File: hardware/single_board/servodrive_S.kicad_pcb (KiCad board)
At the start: 6 copper layers, 65 x 65 mm, 194 parts, among them J1 PhasePad_Arc, J12 USB-C, J13 EXPANSION, J14 RS485 IN, J15 RS485 OUT, J2 PhasePad_Arc, J3 PhasePad_Arc, J4 XT30, Q1 BSC030N08NS5, Q1001 2N7002, Q2 BSC030N08NS5, Q3 BSC030N08NS5, Q4 BSC030N08NS5, Q5 BSC030N08NS5, Q6 BSC030N08NS5, SW1 BOOTSEL, U1 EG2103, U10 MT6701, U11 LMR38010SDDAR, U12 LMR38010SDDAR, U13 USBLC6-2SC6, U14 SIT3088ETK, U15 SIT3088ETK, U17 SIT3088ETK, U18 SIT3088ETK, U2 EG2103, U3 EG2103, U4 INA241A3, U5 INA241A3, U6 INA241A3, U7 RP2350A, U8 W25Q16JVUXIQ, U9 SPX3819M5-3.3, Y1 12MHz

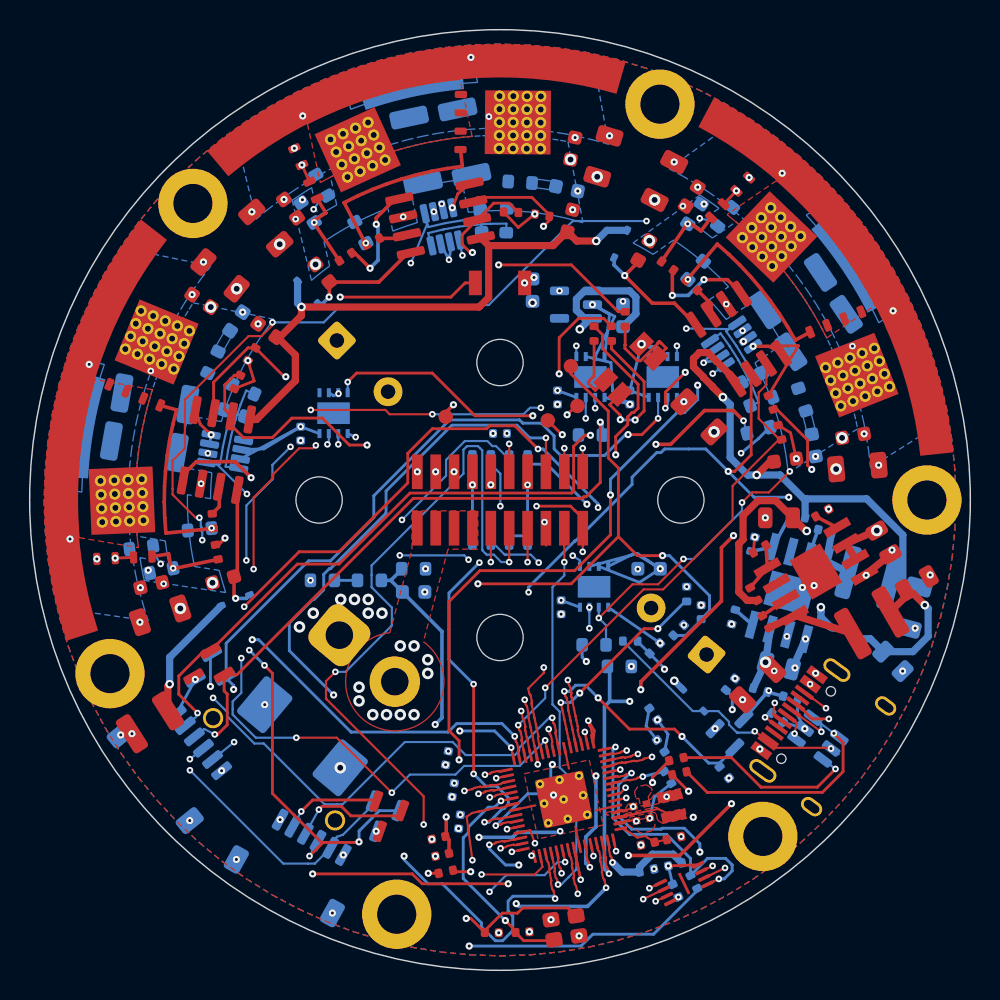
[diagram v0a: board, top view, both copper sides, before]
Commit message: Board S with six D6.3 bulk cans: routed, DRC 0; the bulk options page
The two D10 cans carried 6.4 A of ripple each at 20 A RMS per phase, 3.7
times their rating at 20-40 kHz. Six PA100V22M6X9 (22 uF, 2.6 A) carry
2.3 A each, within rating to 16 A per phase continuously, 0.15 W a can.

Routed with the maze making the RS-485 IN pair and the encoder's CS and DO
before the router, then targeted rip-ups for EXP_GP24, HIN_A and SWCLK.
2241 segments, 444 vias; DRC 0 all severities, ERC 0, parity 219 of the
same kinds as before, netlist diff and deadcheck clean. bulk.html has the
parts, the banks through the DC-link network, what fits and what routed.
ethernet.html: the can holes, and GPIO14 is port OUT's UART now.

Co-Authored-By: Claude Opus 5.5 (1M context) <noreply@anthropic.com>
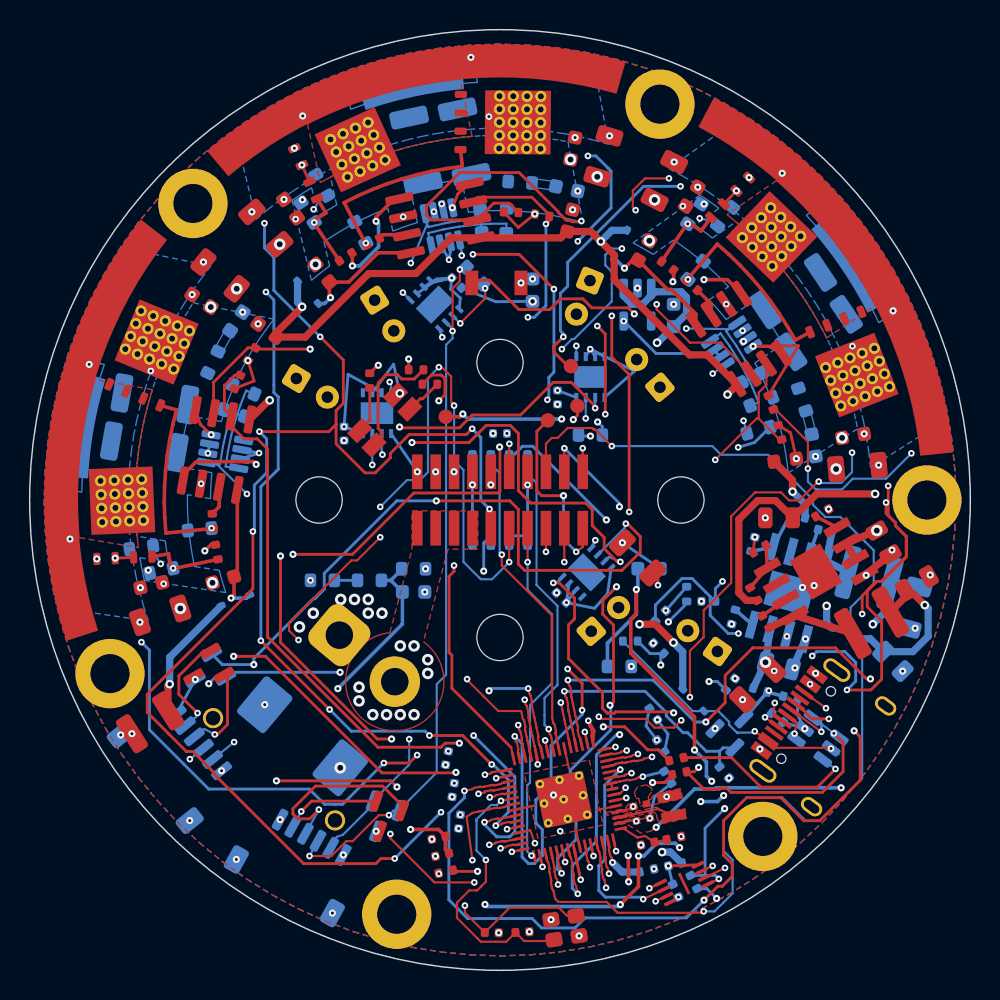
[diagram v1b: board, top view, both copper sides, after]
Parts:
- added C1012: 22u/100V polymer, Capacitor_THT:CP_Radial_D6.3mm_P2.50mm, F.Cu at (139.3, 91.2)
- added C1013: 22u/100V polymer, Capacitor_THT:CP_Radial_D6.3mm_P2.50mm, F.Cu at (154.2, 89.8)
- added C1014: 22u/100V polymer, Capacitor_THT:CP_Radial_D6.3mm_P2.50mm, F.Cu at (159.1, 97.2)
- added C1015: 22u/100V polymer, Capacitor_THT:CP_Radial_D6.3mm_P2.50mm, F.Cu at (154.3, 114.1)
- C1001, C1002: value 100u/100V polymer -> 22u/100V polymer; footprint Capacitor_THT:CP_Radial_D10.0mm_P5.00mm -> Capacitor_THT:CP_Radial_D6.3mm_P2.50mm
- moved R1105 26.8 mm to (146.2, 89.5), turned to 135 degrees
- moved C1102 23.5 mm to (145.0, 90.0), turned to 135 degrees
- moved U14 22.4 mm to (143.5, 91.5), turned to 45 degrees
- moved D1103 17.4 mm to (140.0, 99.5)
- moved R1107 15.8 mm to (139.0, 96.8)
- moved C1104 14.6 mm to (152.2, 111.8), turned to 135 degrees
- moved U17 14.5 mm to (154.0, 110.0), turned to 135 degrees
- moved R1109 14.2 mm to (143.2, 97.0), turned to 0 degrees
- moved R1108 13.7 mm to (142.2, 96.0), turned to 0 degrees
- moved C1007 10.6 mm to (157.5, 109.0)
- moved U9 4.25 mm to (157.5, 91.5), turned to -90 degrees
- moved C1001 3.84 mm to (133.9, 96.6), turned to -31 degrees
- moved C713 3.50 mm to (160.0, 92.2)
- moved C1103 3.00 mm to (137.2, 100.4)
- moved U15 3.00 mm to (139.5, 99.0)
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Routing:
- net RUN: track 60.2 -> 278.3 mm, vias 4 -> 18
- net SWCLK: track 45.6 -> 153.0 mm, vias 7 -> 11
- net RS485_IN_DN_P: track 129.1 -> 44.2 mm, vias 9 -> 3
- net RS485_IN_RX: track 14.4 -> 83.6 mm, vias 2 -> 4
- net ENC_DO: track 83.2 -> 21.5 mm, vias 8 -> 1
- net HIN_A: track 51.4 -> 110.2 mm, vias 5 -> 8
- net SWDIO: track 37.5 -> 95.6 mm, vias 4 -> 11
- net RS485_OUT_TX: track 47.0 -> 92.2 mm
- net RS485_IN_TX: track 48.0 -> 91.1 mm, vias 3 -> 7
- net ENC_SCK: track 69.1 -> 27.6 mm, vias 7 -> 2
- net LED_B: track 84.9 -> 46.3 mm, vias 4 -> 2
- net RS485_OUT_DN_P: track 79.4 -> 53.4 mm
- net RS485_IN_DN_N: track 73.3 -> 49.1 mm, vias 10 -> 4
- net EXP_GP20: track 48.8 -> 28.8 mm, vias 4 -> 2
- net +1V1: track 26.1 -> 45.9 mm, vias 4 -> 7
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
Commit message: Board S: SIT65HVD75ETK and W25Q80DVUXIE for the parts that went out of stock
Every placed part re-checked at JLCPCB on 2026-10-16: the SIT3088ETK and
the W25Q16JVUXIQ were at zero. The SIT65HVD75ETK is the same MAX3485
pinout in the same DFN-8 3x3 (C7433976, 20,671 in stock), and its receiver
threshold (V_IT+ <= -10 mV) reads a terminated idle pair as a 1, which
answers the fail-safe item on paper. The W25Q80DVUXIE is the same pins and
USON 2x3 land pattern, 8 Mbit (C401667, 8,611): firmware needs
PICO_FLASH_SIZE_BYTES 1 MB and has to set QE, which it ships clear.

Board S only (schematic_s overrides; board A keeps the W25Q16JV): two new
derived symbols appended to the library, the two sheets regenerated, the
routed board's value fields patched, the fan-out's escape rule taking the
new name. ERC 0, netlist == schematic_s, DRC 0 / 0 unconnected, schematic
parity the same 219 items as before. Viewer rebuilt.

Still short: the RP2350's 3.3 uH AOTA-B201610S3R3 (9) and TPSMF4L54A (42,
three a board).

Co-Authored-By: Claude Opus 5.5 <noreply@anthropic.com>
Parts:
- U14, U15, U17, U18: value SIT3088ETK -> SIT65HVD75ETK
- U8: value W25Q16JVUXIQ -> W25Q80DVUXIE
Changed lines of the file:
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@@
 			)
 		)
-		(property "Value" "W25Q16JVUXIQ"
+		(property "Value" "W25Q80DVUXIE"
 			(at 0 1.95 0)
 			(layer "F.Fab")
@@
 			)
 		)
-		(property "Value" "SIT3088ETK"
+		(property "Value" "SIT65HVD75ETK"
 			(at 0 0 0)
 			(layer "B.Fab")
@@
 			)
 		)
-		(property "Value" "SIT3088ETK"
+		(property "Value" "SIT65HVD75ETK"
 			(at 0 0 0)
 			(layer "B.Fab")
@@
 			)
 		)
-		(property "Value" "SIT3088ETK"
+		(property "Value" "SIT65HVD75ETK"
 			(at 0 0 0)
 			(layer "B.Fab")
@@
 			)
 		)
-		(property "Value" "SIT3088ETK"
+		(property "Value" "SIT65HVD75ETK"
 			(at 0 0 0)
 			(layer "B.Fab")
